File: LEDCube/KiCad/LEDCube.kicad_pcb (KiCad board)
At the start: 2 copper layers, 70 x 50 mm, 9 parts, among them J1 BARREL_JACK, J2 ICSP HEADER, J3 TO_ANODES, J4 TO_CATHODES, U1 ATMEGA16-16PU, U2 LM7805, U3 ULN2803A

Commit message: Add files via upload
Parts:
- moved U1 51.8 mm to (80.1, 87.8)
- moved C1 51.8 mm to (89.5, 96.5)
- moved J1 51.8 mm to (79.6, 62.1)
- moved J2 51.8 mm to (102.7, 63.2)
- moved J3 51.8 mm to (133.9, 62.5)
- moved J4 51.8 mm to (74.8, 76.3)
- moved C2 51.8 mm to (80.8, 99.8)
- moved U2 51.8 mm to (72.9, 95.0)
- moved U3 51.8 mm to (99.1, 101.8)
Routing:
- net GND: track 149.8 -> 169.2 mm
- net Net-(U1-Pad15): track 22.5 -> 41.1 mm
- net Net-(U1-Pad16): track 22.5 -> 38.3 mm
- net Net-(U1-Pad17): track 22.5 -> 35.6 mm
- net Net-(J4-Pad1): track 36.3 -> 42.9 mm
- net Net-(J4-Pad2): track 34.9 -> 39.5 mm
- net +12V: track 56.2 -> 60.5 mm
- net Net-(J4-Pad3): track 39.2 -> 42.7 mm
- net Net-(J3-Pad3): track 51.7 -> 53.9 mm
- net Net-(J3-Pad4): track 48.4 -> 50.5 mm
- net Net-(J3-Pad2): track 55.3 -> 57.0 mm
- net Net-(J2-Pad3): track 1.42 -> 0.00 mm
- net Net-(J3-Pad1): track 58.9 -> 60.3 mm
- net Net-(J3-Pad5): track 46.6 -> 47.9 mm
- net Net-(J2-Pad9): track 39.7 -> 40.8 mm
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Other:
- net class Default: trace_width 0.25 -> 0.3
- rule trace_min: 0.25 -> 0.3

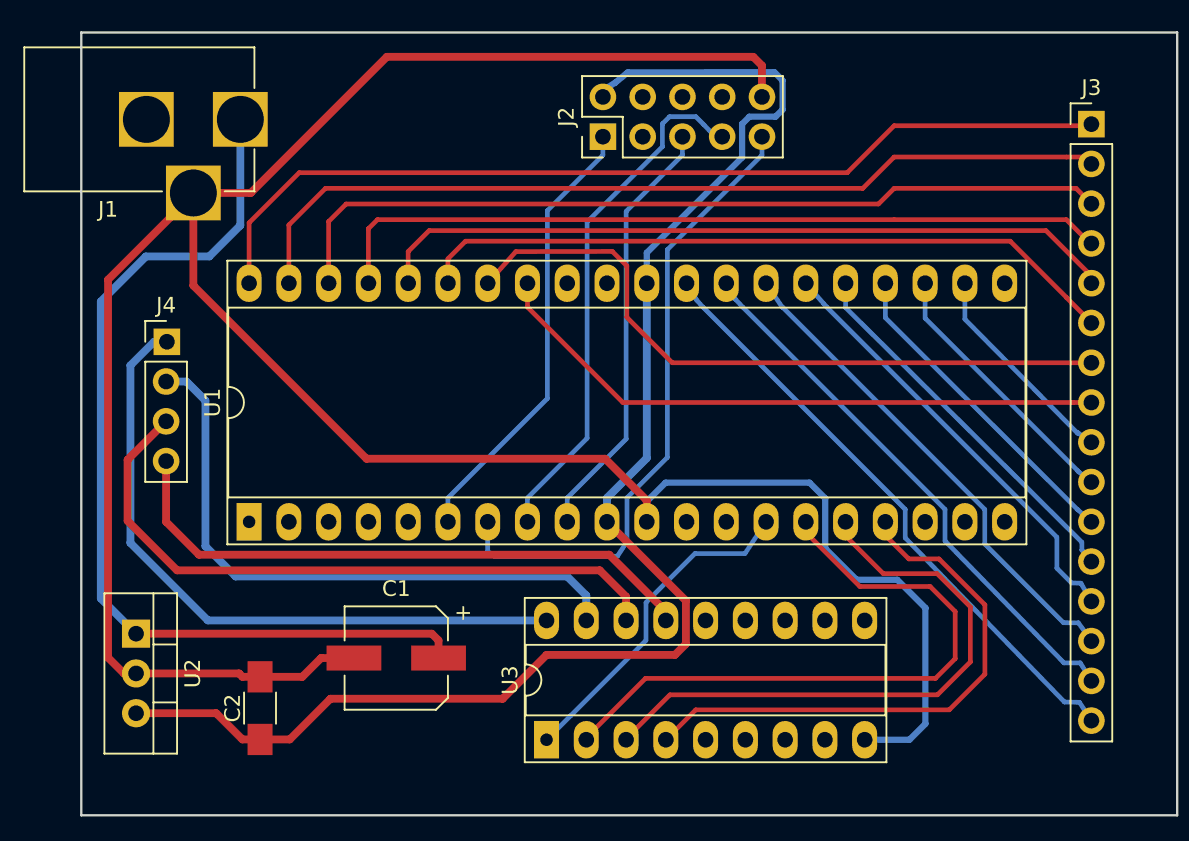
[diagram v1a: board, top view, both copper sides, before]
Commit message: Tracks changed
Tracks and track widths changed.
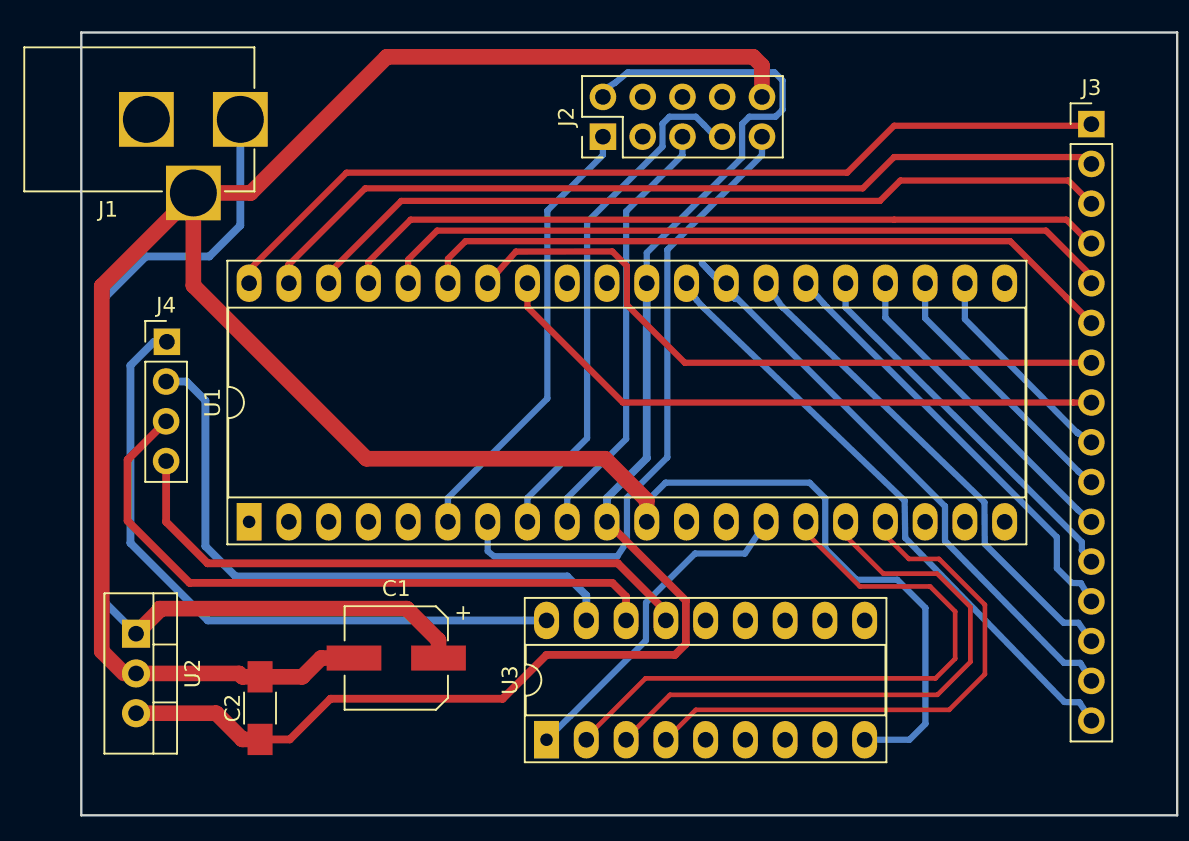
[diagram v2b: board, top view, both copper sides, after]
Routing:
- net Net-(J3-Pad15): track 35.4 -> 41.7 mm
- net Net-(J3-Pad1): track 60.3 -> 58.5 mm
- net Net-(J3-Pad3): track 53.9 -> 52.4 mm
- net Net-(J3-Pad2): track 57.0 -> 55.5 mm
- net +12V: track 60.5 -> 61.9 mm
- net Net-(J3-Pad4): track 50.5 -> 49.3 mm

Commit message: Minor changes
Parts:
- moved U2 14.8 mm to (70.7, 80.4)
- moved U3 14.8 mm to (96.9, 87.1)
- moved J1 14.8 mm to (77.3, 47.5)
- moved J2 14.8 mm to (100.5, 48.6)
- moved J3 14.8 mm to (131.7, 47.8)
- moved C1 14.8 mm to (87.3, 81.9)
- moved C2 14.8 mm to (78.6, 85.1)
- moved J4 14.8 mm to (72.6, 61.7)
- moved U1 14.8 mm to (77.9, 73.2)
